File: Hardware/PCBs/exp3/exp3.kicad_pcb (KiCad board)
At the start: 2 copper layers, 52.1 x 35.6 mm, 8 parts, among them J1 Conn_01x07_Female, J2 Conn_01x06_Female, U1 74HC86, U2 7483

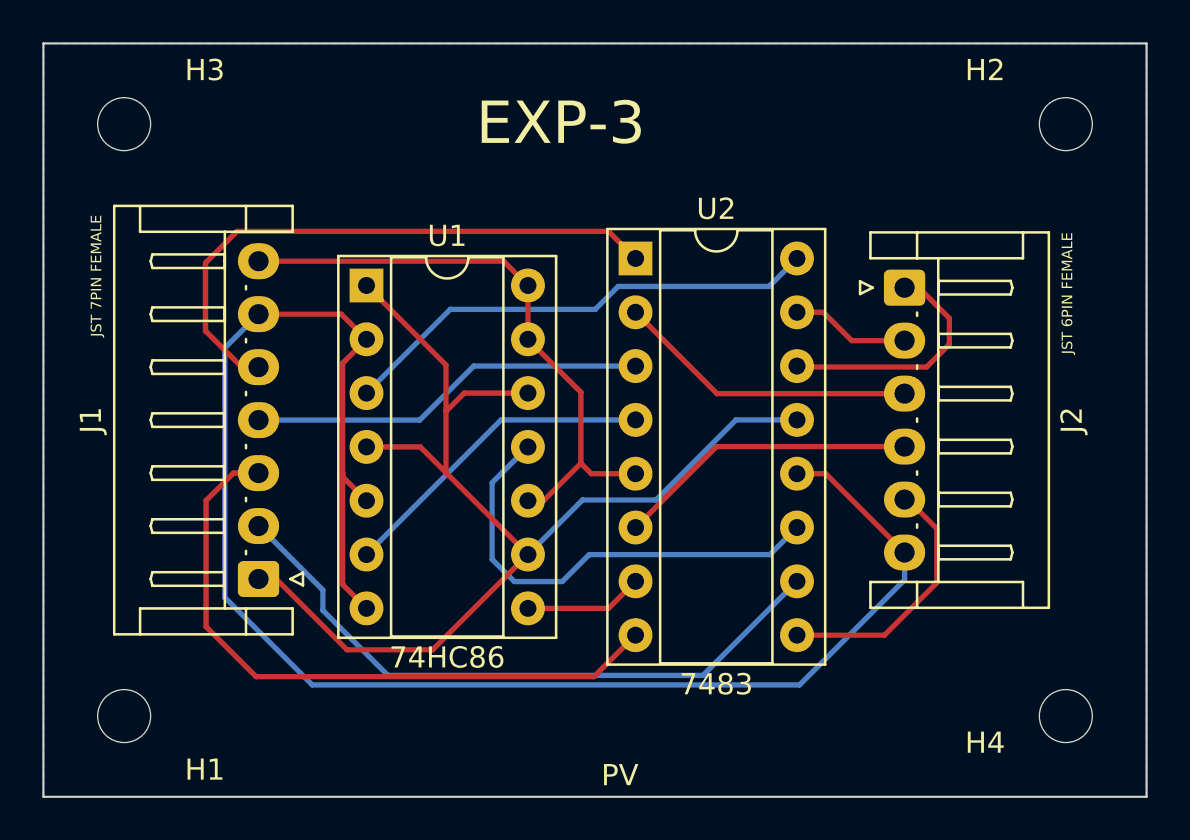
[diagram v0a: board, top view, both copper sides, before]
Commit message: PCBs Updated
pcb of exp1, 2 and 3 updated
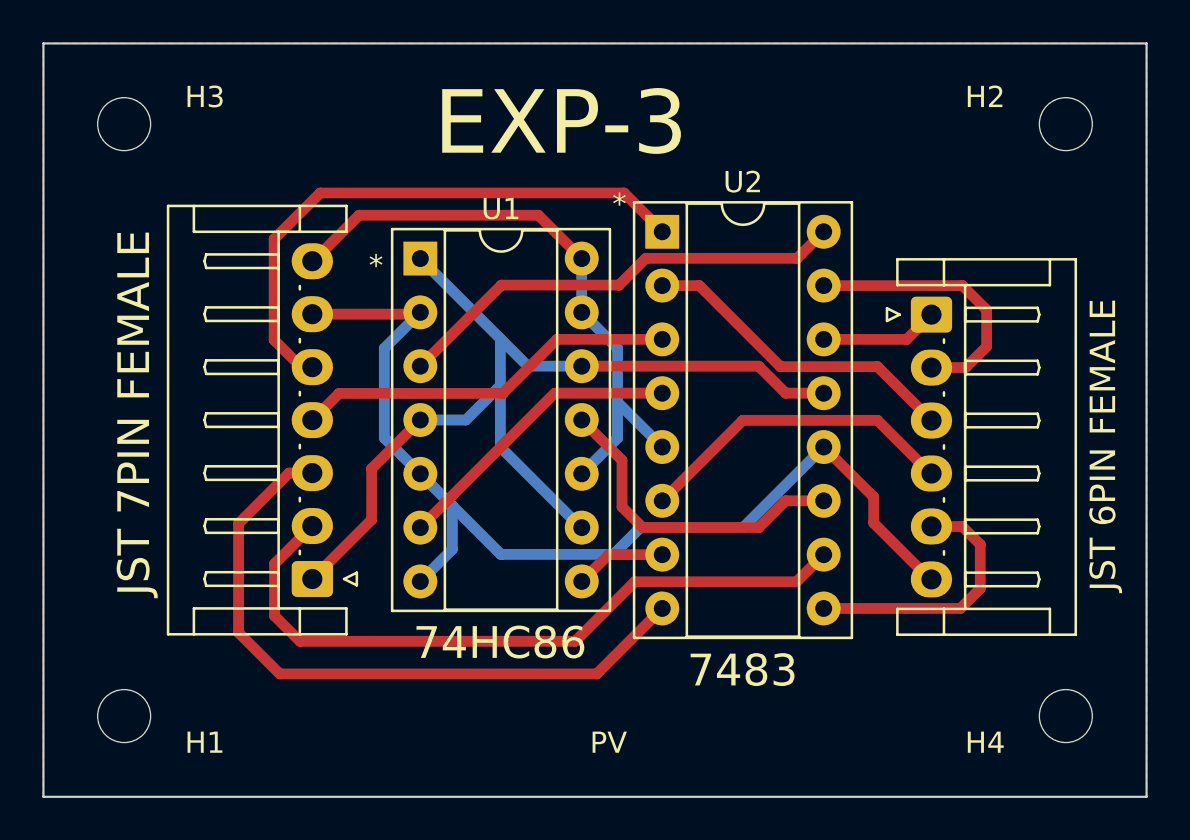
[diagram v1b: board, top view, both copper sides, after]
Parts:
- moved U1 2.84 mm to (124.5, 87.6)
- moved J1 2.54 mm to (119.4, 102.8)
- moved J2 1.80 mm to (148.6, 90.3)
- moved U2 1.78 mm to (135.9, 86.4)
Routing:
- net GND: track 78.8 -> 49.4 mm
- net Cin: track 55.6 -> 46.2 mm
- net S3: track 5.63 -> 12.9 mm
- net Net-(U1-Pad11): track 21.9 -> 15.3 mm
- net CO: track 11.6 -> 5.57 mm
- net A0: track 30.7 -> 33.1 mm
- net VCC: track 28.6 -> 30.7 mm
- net Net-(U1-Pad6): track 15.3 -> 14.0 mm
- net Net-(U1-Pad8): track 5.61 -> 4.32 mm
- net Net-(U1-Pad3): track 23.0 -> 21.7 mm
- net S2: track 14.3 -> 15.3 mm
- net S1: track 14.3 -> 15.3 mm
- net A3: track 27.9 -> 27.1 mm
- net A2: track 18.9 -> 18.1 mm
- net A1: track 31.0 -> 31.7 mm
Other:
- board text added: "*"

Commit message: Exp - 2 and 3 PCB Updated
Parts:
- moved U1 1.28 mm to (124.5, 88.9)
- moved J2 0.25 mm to (148.6, 90.0)
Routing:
- net A1: track 31.7 -> 21.8 mm
- net A0: track 33.1 -> 24.7 mm
- net A3: track 27.1 -> 19.2 mm
- net S3: track 12.9 -> 6.58 mm
- net Cin: track 46.2 -> 52.0 mm
- net S0: track 12.5 -> 6.79 mm
- net Net-(U1-Pad11): track 15.3 -> 12.5 mm
- net GND: track 49.4 -> 51.8 mm
- net S1: track 15.3 -> 14.3 mm
- net VCC: track 30.7 -> 30.1 mm
- net Net-(U1-Pad3): track 21.7 -> 22.2 mm
- net Net-(U1-Pad8): track 4.32 -> 4.87 mm
- net Net-(U1-Pad6): track 14.0 -> 14.6 mm

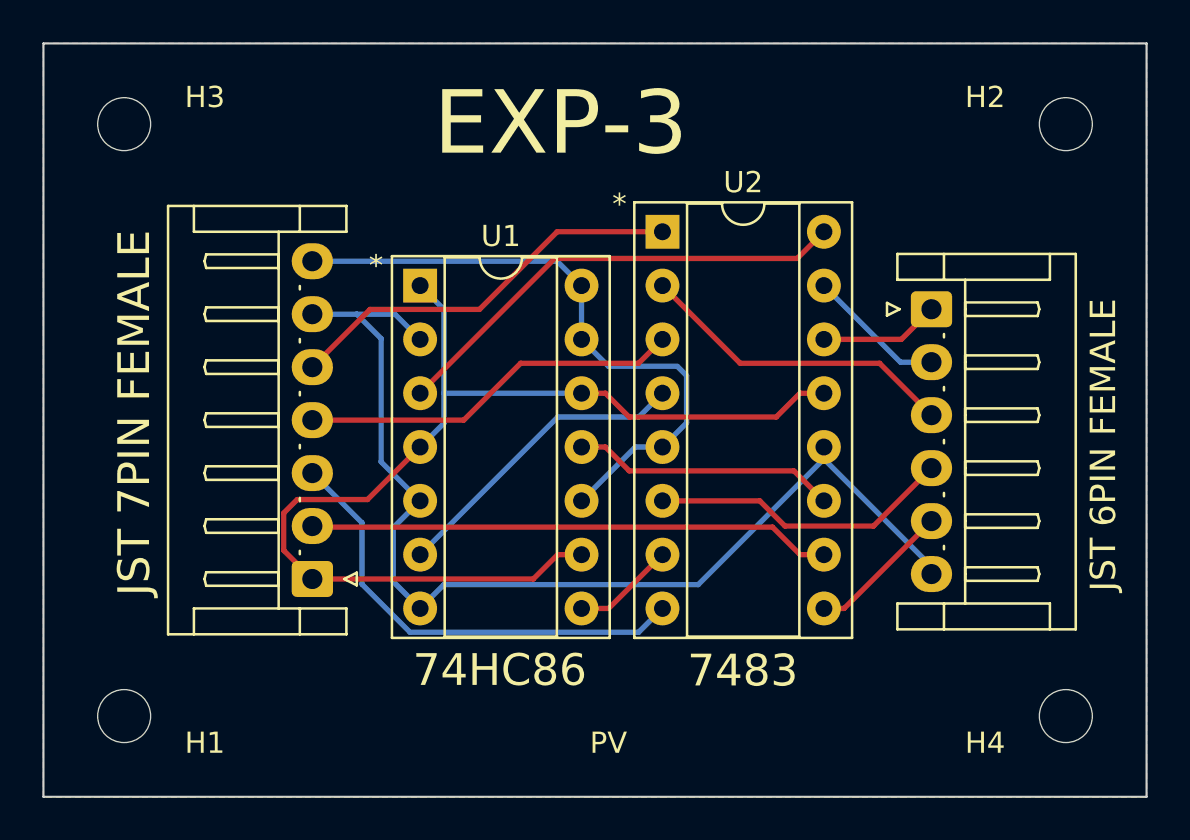
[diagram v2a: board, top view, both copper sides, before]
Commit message: exp 3 PCB updated
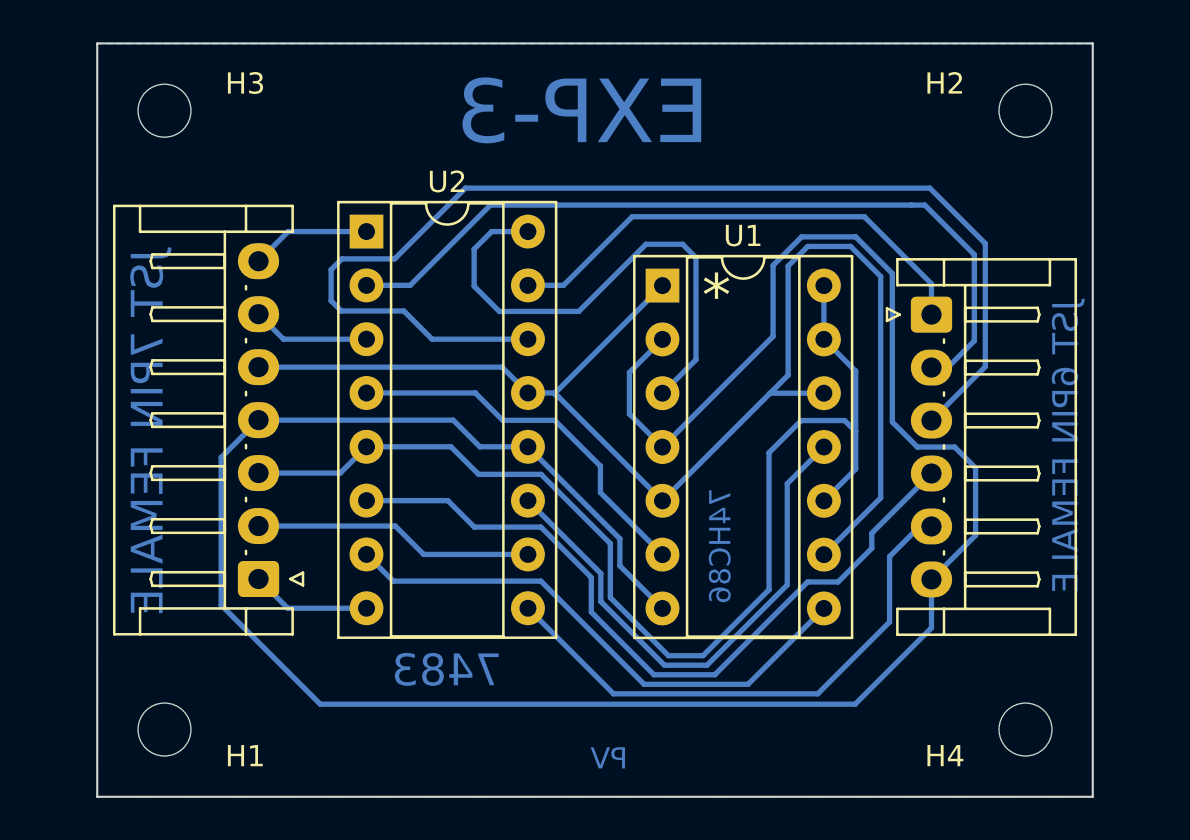
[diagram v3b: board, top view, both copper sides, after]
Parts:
- moved U2 14.0 mm to (121.9, 86.3)
- moved U1 11.4 mm to (135.9, 88.9)
- moved J1 2.54 mm to (116.8, 102.8)
- moved H1 2.01 mm to (112.4, 109.9)
- moved H2 2.01 mm to (153.0, 80.6)
- moved H3 2.01 mm to (112.4, 80.6)
- moved H4 2.01 mm to (153.0, 109.9)
- moved J2 0.25 mm to (148.6, 90.3)
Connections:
- J1 pad 1: Cin -> A1
- J1 pad 3: A1 -> VCC
- J1 pad 4: A2 -> GND
- J1 pad 5: A3 -> Cin
- J1 pad 6: GND -> A2
- J1 pad 7: VCC -> A3
- J2 pad 1: CO -> S3
- J2 pad 2: S3 -> S2
- J2 pad 3: S2 -> CO
- U1 pad 4: Cin -> GND
- U1 pad 5: GND -> Cin
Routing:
- net GND: track 51.8 -> 114.2 mm
- net CO: track 5.67 -> 54.5 mm
- net VCC: track 30.1 -> 54.3 mm
- net S2: track 15.2 -> 37.8 mm
- net S1: track 14.3 -> 35.4 mm
- net Net-(U1-Pad8): track 4.87 -> 25.6 mm
- net S0: track 6.79 -> 25.8 mm
- net S3: track 6.58 -> 23.2 mm
- net A1: track 21.8 -> 5.67 mm
- net A3: track 19.2 -> 5.68 mm
- net Cin: track 52.0 -> 64.6 mm
- net Net-(U1-Pad11): track 12.5 -> 25.0 mm
- net A2: track 18.1 -> 5.59 mm
- net A0: track 24.7 -> 13.3 mm
- net Net-(U1-Pad6): track 14.6 -> 17.9 mm
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- removed copper zone on F.Cu, net (none)
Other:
- board size 52.1 x 35.6 mm -> 47 x 35.6 mm

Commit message: PCBs Updated
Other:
- board text added: "A0"
- board text added: "A1"
- board text added: "A2"
- board text added: "A3"
- board text added: "C0"
- board text added: "Cin"
- board text added: "GND"
- board text added: "Gnd"
- board text added: "S0"
- board text added: "S1"
- board text added: "S2"
- board text added: "S3"
- board text added: "Vcc"
- board text removed: "JST 6PIN FEMALE"
- board text removed: "JST 7PIN FEMALE"
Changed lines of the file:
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@@
     (fp_line (start 17.5 1.5) (end 16.5 1.5) (layer "F.Fab") (width 0.1))
     (fp_line (start -2.5 -6.7) (end 17.5 -6.7) (layer "F.Fab") (width 0.1))
-    (pad "1" thru_hole roundrect (at 0 0 90) (size 1.7 1.95) (drill 0.95) (layers *.Cu *.Mask) (roundrect_rratio 0.1470588235)
+    (pad "1" thru_hole roundrect (at 0 0 90) (size 1.7 1.95) (drill 1.2) (layers *.Cu *.Mask) (roundrect_rratio 0.1470588235)
       (net 3 "A1") (pinfunction "Pin_1") (pintype "passive"))
-    (pad "2" thru_hole oval (at 2.5 0 90) (size 1.7 1.95) (drill 0.95) (layers *.Cu *.Mask)
+    (pad "2" thru_hole oval (at 2.5 0 90) (size 1.7 1.95) (drill 1.2) (layers *.Cu *.Mask)
       (net 2 "A0") (pinfunction "Pin_2") (pintype "passive"))
-    (pad "3" thru_hole oval (at 5 0 90) (size 1.7 1.95) (drill 0.95) (layers *.Cu *.Mask)
+    (pad "3" thru_hole oval (at 5 0 90) (size 1.7 1.95) (drill 1.2) (layers *.Cu *.Mask)
       (net 15 "VCC") (pinfunction "Pin_3") (pintype "passive"))
-    (pad "4" thru_hole oval (at 7.5 0 90) (size 1.7 1.95) (drill 0.95) (layers *.Cu *.Mask)
+    (pad "4" thru_hole oval (at 7.5 0 90) (size 1.7 1.95) (drill 1.2) (layers *.Cu *.Mask)
       (net 6 "GND") (pinfunction "Pin_4") (pintype "passive"))
-    (pad "5" thru_hole oval (at 10 0 90) (size 1.7 1.95) (drill 0.95) (layers *.Cu *.Mask)
+    (pad "5" thru_hole oval (at 10 0 90) (size 1.7 1.95) (drill 1.2) (layers *.Cu *.Mask)
       (net 1 "Cin") (pinfunction "Pin_5") (pintype "passive"))
-    (pad "6" thru_hole oval (at 12.5 0 90) (size 1.7 1.95) (drill 0.95) (layers *.Cu *.Mask)
+    (pad "6" thru_hole oval (at 12.5 0 90) (size 1.7 1.95) (drill 1.2) (layers *.Cu *.Mask)
       (net 4 "A2") (pinfunction "Pin_6") (pintype "passive"))
-    (pad "7" thru_hole oval (at 15 0 90) (size 1.7 1.95) (drill 0.95) (layers *.Cu *.Mask)
+    (pad "7" thru_hole oval (at 15 0 90) (size 1.7 1.95) (drill 1.2) (layers *.Cu *.Mask)
       (net 5 "A3") (pinfunction "Pin_7") (pintype "passive"))
     (model "${KICAD6_3DMODEL_DIR}/Connector_JST.3dshapes/JST_EH_S7B-EH_1x07_P2.50mm_Horizontal.wrl"
@@
     (fp_line (start -1.5 -0.7) (end -1.5 1.5) (layer "F.Fab") (width 0.1))
     (fp_line (start -2.5 -6.7) (end 15 -6.7) (layer "F.Fab") (width 0.1))
-    (pad "1" thru_hole roundrect (at 0 0 270) (size 1.7 1.95) (drill 0.95) (layers *.Cu *.Mask) (roundrect_rratio 0.1470588235)
+    (pad "1" thru_hole roundrect (at 0 0 270) (size 1.7 1.95) (drill 1.2) (layers *.Cu *.Mask) (roundrect_rratio 0.1470588235)
       (net 8 "S3") (pinfunction "Pin_1") (pintype "passive"))
-    (pad "2" thru_hole oval (at 2.5 0 270) (size 1.7 1.95) (drill 0.95) (layers *.Cu *.Mask)
+    (pad "2" thru_hole oval (at 2.5 0 270) (size 1.7 1.95) (drill 1.2) (layers *.Cu *.Mask)
       (net 9 "S2") (pinfunction "Pin_2") (pintype "passive"))
-    (pad "3" thru_hole oval (at 5 0 270) (size 1.7 1.95) (drill 0.95) (layers *.Cu *.Mask)
+    (pad "3" thru_hole oval (at 5 0 270) (size 1.7 1.95) (drill 1.2) (layers *.Cu *.Mask)
       (net 7 "CO") (pinfunction "Pin_3") (pintype "passive"))
-    (pad "4" thru_hole oval (at 7.5 0 270) (size 1.7 1.95) (drill 0.95) (layers *.Cu *.Mask)
+    (pad "4" thru_hole oval (at 7.5 0 270) (size 1.7 1.95) (drill 1.2) (layers *.Cu *.Mask)
       (net 10 "S1") (pinfunction "Pin_4") (pintype "passive"))
-    (pad "5" thru_hole oval (at 10 0 270) (size 1.7 1.95) (drill 0.95) (layers *.Cu *.Mask)
+    (pad "5" thru_hole oval (at 10 0 270) (size 1.7 1.95) (drill 1.2) (layers *.Cu *.Mask)
       (net 11 "S0") (pinfunction "Pin_5") (pintype "passive"))
-    (pad "6" thru_hole oval (at 12.5 0 270) (size 1.7 1.95) (drill 0.95) (layers *.Cu *.Mask)
+    (pad "6" thru_hole oval (at 12.5 0 270) (size 1.7 1.95) (drill 1.2) (layers *.Cu *.Mask)
       (net 6 "GND") (pinfunction "Pin_6") (pintype "passive"))
     (model "${KICAD6_3DMODEL_DIR}/Connector_JST.3dshapes/JST_EH_S6B-EH_1x06_P2.50mm_Horizontal.wrl"
@@
     )
     (fp_text value "74HC86" (at 2.74 12.29 90) (layer "B.Cu")
-      (effects (font (size 1 1) (thickness 0.25)) (justify mirror))
+      (effects (font (size 1 1) (thickness 0.15)) (justify mirror))
     )
     (fp_text user "${REFERENCE}" (at 3.81 7.62) (layer "F.Fab")
@@
   (gr_line (start 156.21 113.03) (end 109.22 113.03) (layer "Edge.Cuts") (width 0.1))
   (gr_line (start 156.21 77.47) (end 156.21 113.03) (layer "Edge.Cuts") (width 0.1))
-  (gr_text "JST 6PIN FEMALE" (at 154.94 96.52 90) (layer "B.Cu")
-    (effects (font (size 1.2 1.2) (thickness 0.25)) (justify mirror))
-  )
-  (gr_text "JST 7PIN FEMALE " (at 111.61 95.85 90) (layer "B.Cu")
-    (effects (font (size 1.5 1.5) (thickness 0.25)) (justify mirror))
+  (gr_text "S3" (at 152.9588 90.297 90) (layer "B.Cu")
+    (effects (font (size 1 1) (thickness 0.15)) (justify mirror))
+  )
+  (gr_text "S2" (at 152.9588 92.7354 90) (layer "B.Cu")
+    (effects (font (size 1 1) (thickness 0.15)) (justify mirror))
+  )
+  (gr_text "A3" (at 112.0902 87.6808 270) (layer "B.Cu")
+    (effects (font (size 1 1) (thickness 0.15)) (justify mirror))
+  )
+  (gr_text "Gnd" (at 112.649 95.1738) (layer "B.Cu")
+    (effects (font (size 1 1) (thickness 0.15)) (justify mirror))
+  )
+  (gr_text "Cin" (at 112.4458 92.71) (layer "B.Cu")
+    (effects (font (size 1 1) (thickness 0.15)) (justify mirror))
+  )
+  (gr_text "GND" (at 152.781 102.9208) (layer "B.Cu")
+    (effects (font (size 1 1) (thickness 0.15)) (justify mirror))
+  )
+  (gr_text "A0" (at 112.1664 100.3046) (layer "B.Cu")
+    (effects (font (size 1 1) (thickness 0.15)) (justify mirror))
   )
   (gr_text "EXP-3" (at 132.13 80.74) (layer "B.Cu")
     (effects (font (size 3 3) (thickness 0.3)) (justify mirror))
   )
+  (gr_text "S0" (at 153.035 100.2538 90) (layer "B.Cu")
+    (effects (font (size 1 1) (thickness 0.15)) (justify mirror))
+  )
+  (gr_text "C0" (at 152.9842 95.3262 90) (layer "B.Cu")
+    (effects (font (size 1 1) (thickness 0.15)) (justify mirror))
+  )
+  (gr_text "Vcc" (at 112.5474 97.6122) (layer "B.Cu")
+    (effects (font (size 1 1) (thickness 0.15)) (justify mirror))
+  )
+  (gr_text "A1" (at 112.1918 102.7176) (layer "B.Cu")
+    (effects (font (size 1 1) (thickness 0.15)) (justify mirror))
+  )
+  (gr_text "S1" (at 153.035 97.8408 90) (layer "B.Cu")
+    (effects (font (size 1 1) (thickness 0.15)) (justify mirror))
+  )
+  (gr_text "A2" (at 112.1156 90.2716 270) (layer "B.Cu")
+    (effects (font (size 1 1) (thickness 0.15)) (justify mirror))
+  )
   (gr_text "PV\n" (at 133.38 111.23) (layer "B.Cu")
